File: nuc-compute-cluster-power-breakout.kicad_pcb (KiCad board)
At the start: 4 copper layers, 100 x 100 mm, 169 parts, among them J1 USB3106-30-0230-A, J10 10107844-002LF, J2 BM04B-SRSS-TB-LF-SN, J3 BM04B-SRSS-TB-LF-SN, J4 43045-1013, J5 430450812, J6 430450812, J7 430450812, J8 430450812, J9 430450812, Q1 SQS401EN-T1_BE3, Q10 SSM3K15ACT, Q11 BC856,215, Q2 SQS401EN-T1_BE3, Q3 SSM3K15ACT, Q4 SSM3K15ACT, Q5 SQS401EN-T1_BE3, Q6 SSM3K15ACT, Q7 SQS401EN-T1_BE3, Q8 SQS401EN-T1_BE3, Q9 SSM3K15ACT, U1 FT2232HL-REEL, U10 TCA9534, U11 TMCS1100A2-Q1, U12 TMCS1100A2-Q1, U13 TMCS1100A2-Q1, U14 ADS7828, U15 AP62301WU-7, U2 ISO1641, U3 NCP163ASN330T1G, U4 AP62301WU-7, U8 TMCS1100A2-Q1, U9 TMCS1100A2-Q1, Y1 KX-7_12,MHz

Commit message: Performed loclib
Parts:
- C16, C18, C19, C20: footprint antmicro-footprints:0402-cap -> nuc-compute-cluster-power-breakout-footprints:0402-cap
- N1: footprint antmicro-footprints:OSHW-Logo_7.5x8mm_Mask -> nuc-compute-cluster-power-breakout-footprints:OSHW-Logo_7.5x8mm_Mask
- N2: footprint antmicro-footprints:antmicro-logo_scaled_20mm_mask -> nuc-compute-cluster-power-breakout-footprints:antmicro-logo_scaled_20mm_mask
- R11, R12, R36, R37: footprint antmicro-footprints:0402-res -> nuc-compute-cluster-power-breakout-footprints:0402-res
- TP_S1, TP_S10, TP_S11, TP_S12, TP_S16, TP_S17, TP_S18, TP_S19, TP_S2, TP_S20, TP_S21, TP_S22, TP_S23, TP_S24, TP_S3, TP_S4, TP_S5, TP_S6, TP_S7, TP_S8, TP_S9, TP_S_ON1: footprint antmicro-footprints:Testpoint_smd_1mm -> nuc-compute-cluster-power-breakout-footprints:Testpoint_smd_1mm
- U14: footprint antmicro-footprints:TSSOP-16_4.4x5mm_P0.65mm -> nuc-compute-cluster-power-breakout-footprints:TSSOP-16_4.4x5mm_P0.65mm
- U2: footprint antmicro-footprints:SOIC-8_W3.9mm -> nuc-compute-cluster-power-breakout-footprints:SOIC-8_W3.9mm
- U3: footprint antmicro-footprints:SOT-23-5 -> nuc-compute-cluster-power-breakout-footprints:SOT-23-5

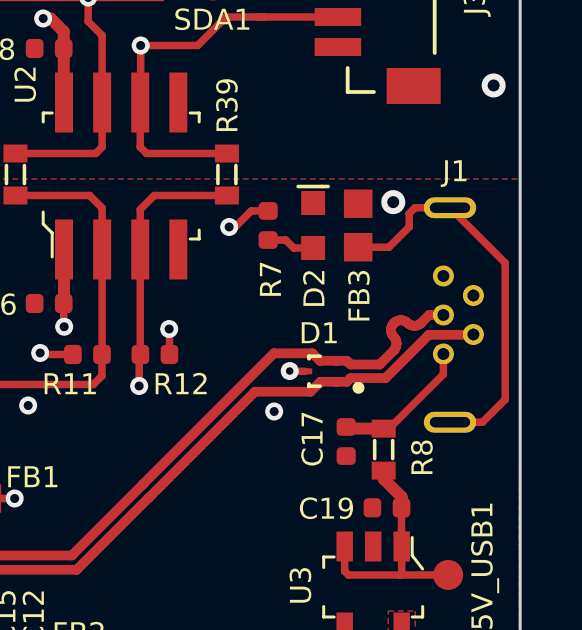
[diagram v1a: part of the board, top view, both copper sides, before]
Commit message: Update USB port footprint
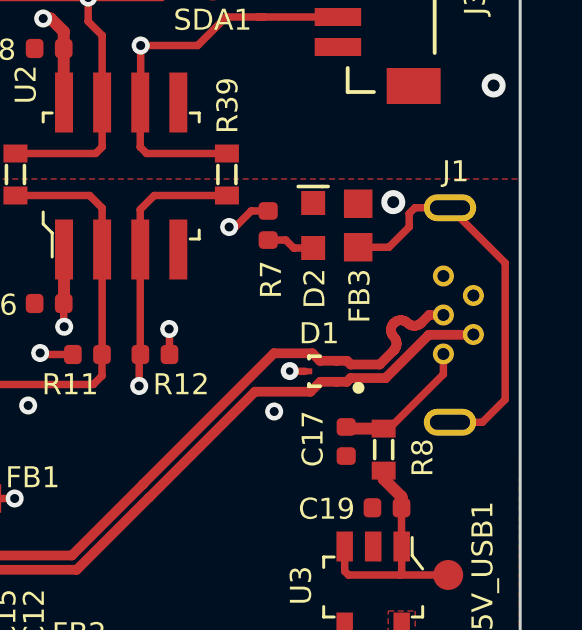
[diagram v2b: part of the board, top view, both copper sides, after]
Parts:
- C16, C18, C19, C20: footprint nuc-compute-cluster-power-breakout-footprints:0402-cap -> antmicro-footprints:0402-cap
- N1: footprint nuc-compute-cluster-power-breakout-footprints:OSHW-Logo_7.5x8mm_Mask -> antmicro-footprints:OSHW-Logo_7.5x8mm_Mask
- N2: footprint nuc-compute-cluster-power-breakout-footprints:antmicro-logo_scaled_20mm_mask -> antmicro-footprints:antmicro-logo_scaled_20mm_mask
- R11, R12, R36, R37: footprint nuc-compute-cluster-power-breakout-footprints:0402-res -> antmicro-footprints:0402-res
- TP_S1, TP_S10, TP_S11, TP_S12, TP_S16, TP_S17, TP_S18, TP_S19, TP_S2, TP_S20, TP_S21, TP_S22, TP_S23, TP_S24, TP_S3, TP_S4, TP_S5, TP_S6, TP_S7, TP_S8, TP_S9, TP_S_ON1: footprint nuc-compute-cluster-power-breakout-footprints:Testpoint_smd_1mm -> antmicro-footprints:Testpoint_smd_1mm
- U14: footprint nuc-compute-cluster-power-breakout-footprints:TSSOP-16_4.4x5mm_P0.65mm -> antmicro-footprints:TSSOP-16_4.4x5mm_P0.65mm
- U2: footprint nuc-compute-cluster-power-breakout-footprints:SOIC-8_W3.9mm -> antmicro-footprints:SOIC-8_W3.9mm
- U3: footprint nuc-compute-cluster-power-breakout-footprints:SOT-23-5 -> antmicro-footprints:SOT-23-5

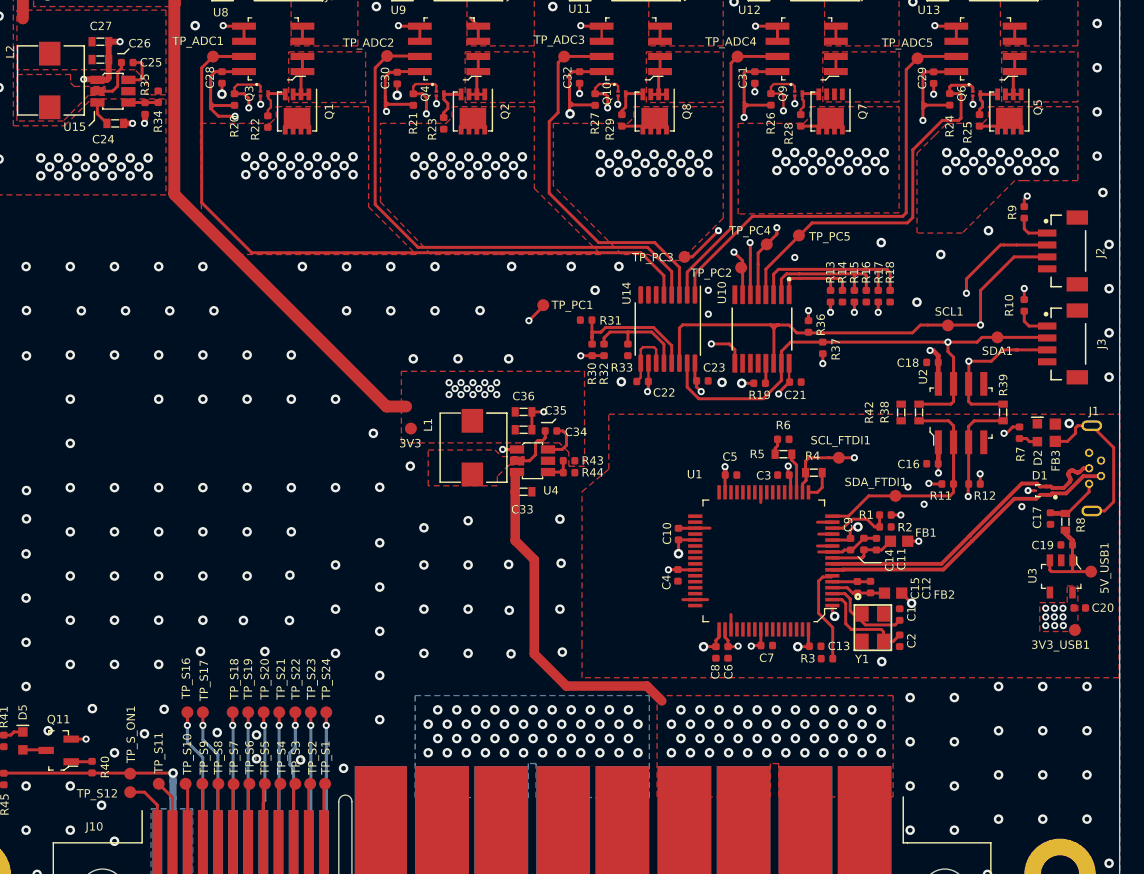
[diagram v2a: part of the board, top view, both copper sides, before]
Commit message: Transistors orientation fix
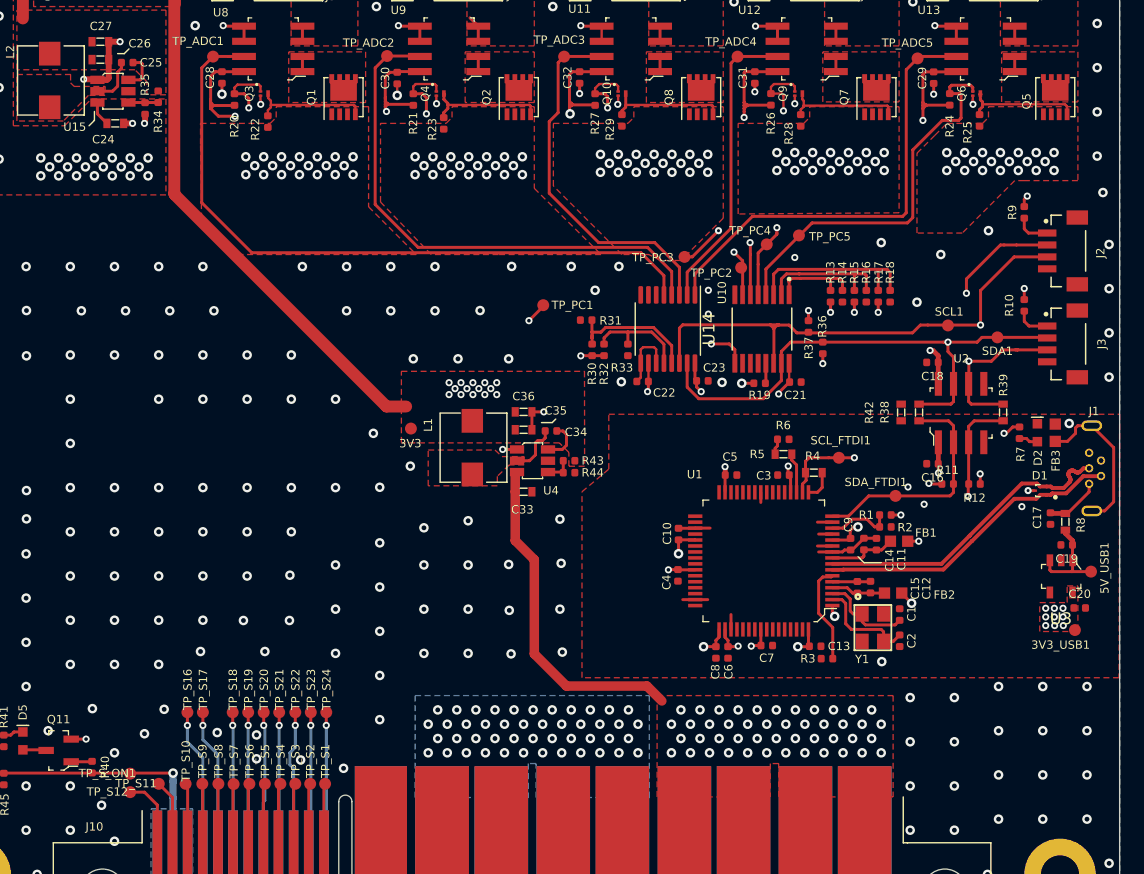
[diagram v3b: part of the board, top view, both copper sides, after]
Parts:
- C16, C18, C19, C20: footprint antmicro-footprints:0402-cap -> nuc-compute-cluster-power-breakout-footprints:0402-cap
- R11, R12, R36, R37: footprint antmicro-footprints:0402-res -> nuc-compute-cluster-power-breakout-footprints:0402-res
- TP_S1, TP_S10, TP_S11, TP_S12, TP_S16, TP_S17, TP_S18, TP_S19, TP_S2, TP_S20, TP_S21, TP_S22, TP_S23, TP_S24, TP_S3, TP_S4, TP_S5, TP_S6, TP_S7, TP_S8, TP_S9, TP_S_ON1: footprint antmicro-footprints:Testpoint_smd_1mm -> nuc-compute-cluster-power-breakout-footprints:Testpoint_smd_1mm
- U14: footprint antmicro-footprints:TSSOP-16_4.4x5mm_P0.65mm -> nuc-compute-cluster-power-breakout-footprints:TSSOP-16_4.4x5mm_P0.65mm
- U2: footprint antmicro-footprints:SOIC-8_W3.9mm -> nuc-compute-cluster-power-breakout-footprints:SOIC-8_W3.9mm
- U3: footprint antmicro-footprints:SOT-23-5 -> nuc-compute-cluster-power-breakout-footprints:SOT-23-5
- moved Q1 4.08 mm to (124.9, 79.8), turned to 90 degrees
- moved Q8 4.08 mm to (154.9, 79.8), turned to 90 degrees
- moved Q2 4.03 mm to (139.6, 79.8), turned to 90 degrees
- moved Q5 4.03 mm to (184.6, 79.8), turned to 90 degrees
- moved Q7 4.03 mm to (169.6, 79.8), turned to 90 degrees
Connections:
- Q1 pad 1: C_MEAS_1 -> VCC12V0
- Q1 pad 2: C_MEAS_1 -> VCC12V0
- Q1 pad 3: C_MEAS_1 -> VCC12V0
- Q1 pad 5: VCC12V0 -> C_MEAS_1
- Q2 pad 1: C_MEAS_2 -> VCC12V0
- Q2 pad 2: C_MEAS_2 -> VCC12V0
- Q2 pad 3: C_MEAS_2 -> VCC12V0
- Q2 pad 5: VCC12V0 -> C_MEAS_2
- Q5 pad 1: C_MEAS_5 -> VCC12V0
- Q5 pad 2: C_MEAS_5 -> VCC12V0
- Q5 pad 3: C_MEAS_5 -> VCC12V0
- Q5 pad 5: VCC12V0 -> C_MEAS_5
- Q7 pad 1: C_MEAS_4 -> VCC12V0
- Q7 pad 2: C_MEAS_4 -> VCC12V0
- Q7 pad 3: C_MEAS_4 -> VCC12V0
- Q7 pad 5: VCC12V0 -> C_MEAS_4
- Q8 pad 1: C_MEAS_3 -> VCC12V0
- Q8 pad 2: C_MEAS_3 -> VCC12V0
- Q8 pad 3: C_MEAS_3 -> VCC12V0
- Q8 pad 5: VCC12V0 -> C_MEAS_3
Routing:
- net VCC12V0: track 57.0 -> 47.8 mm
- net Net-(Q7-Pad4): track 3.32 -> 10.2 mm
- net Net-(Q10-Pad3): track 3.37 -> 9.98 mm
- net Net-(Q5-Pad4): track 3.51 -> 9.96 mm
- net Net-(Q1-Pad4): track 3.53 -> 9.88 mm
- net Net-(Q2-Pad4): track 3.77 -> 10.1 mm
- net C_MEAS_2: track 4.72 -> 1.44 mm
- net C_MEAS_5: track 4.55 -> 1.44 mm
- net C_MEAS_3: track 4.55 -> 1.44 mm
- net C_MEAS_1: track 4.55 -> 1.44 mm
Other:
- board text added: "Rev. 1.1.0"
- board text removed: "Rev. 1.0.0"

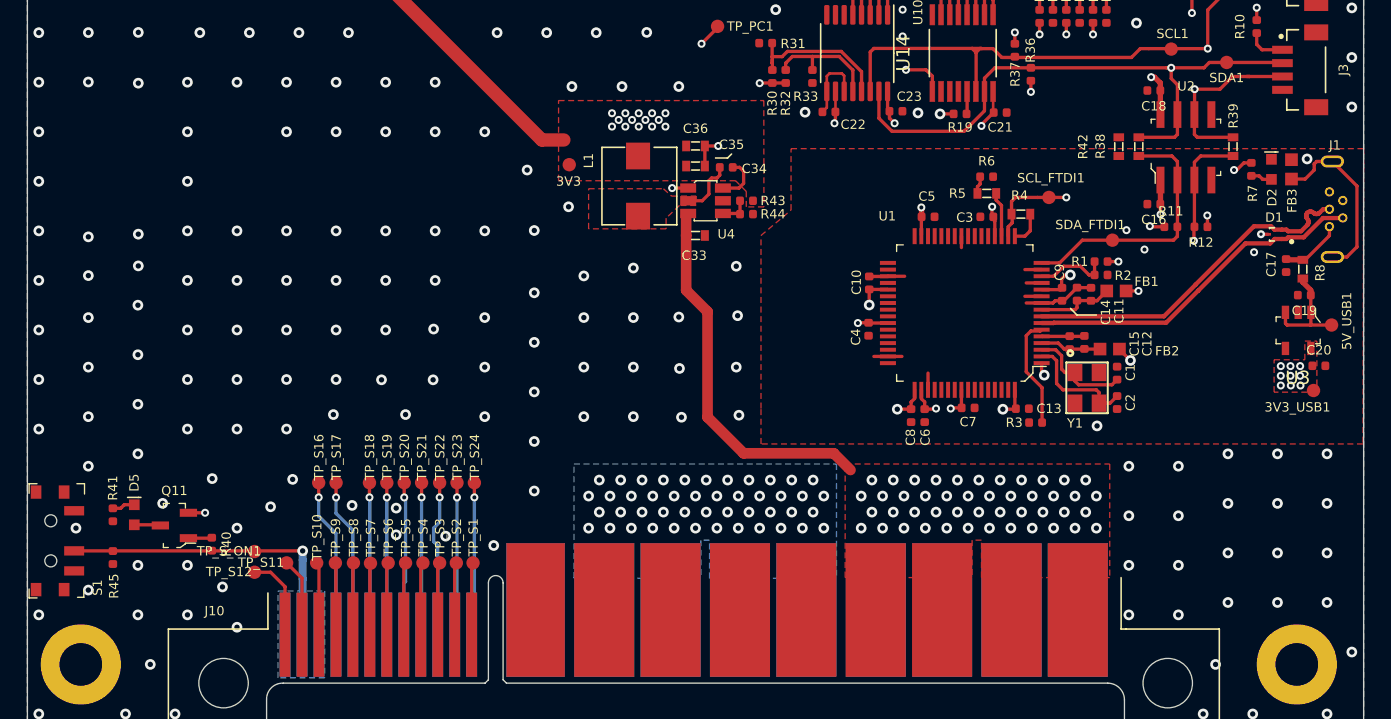
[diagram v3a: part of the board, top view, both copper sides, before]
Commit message: Fixed swapped I2C lines Corrected silkscreen layer Rearranged EdgeConn test points
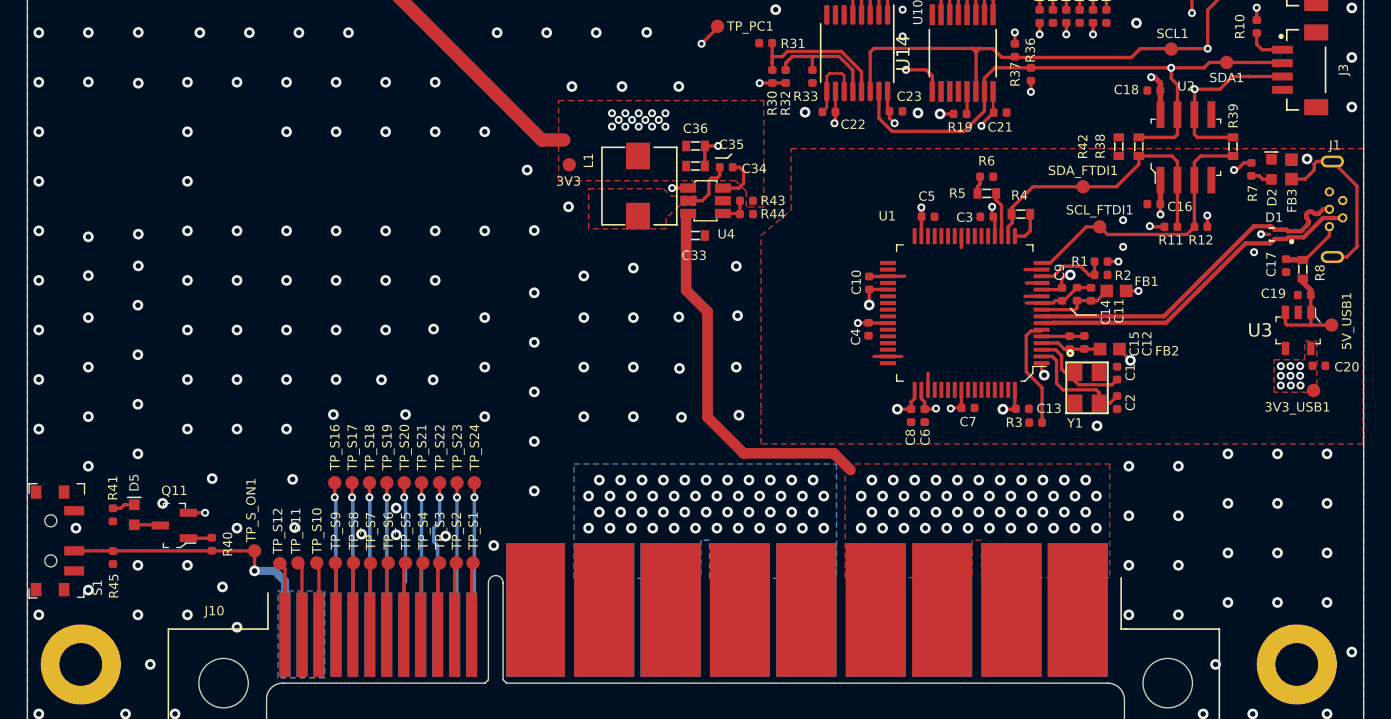
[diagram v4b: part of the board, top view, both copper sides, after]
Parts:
- moved SDA_FTDI1 4.56 mm to (169.0, 109.3)
- moved SCL_FTDI1 4.39 mm to (170.2, 112.3)
- moved TP_S12 2.01 mm to (108.9, 137.5)
- moved TP_S16 1.20 mm to (112.9, 131.4)
- moved TP_S17 1.20 mm to (114.2, 131.4)
- moved TP_S11 0.85 mm to (110.2, 137.5)
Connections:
- R4 pad 2: SCL_FTDI -> SDA_FTDI
- U1 pad 16: SDA_FTDI -> SCL_FTDI
- U1 pad 18: SCL_FTDI -> SDA_FTDI
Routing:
- net SCL_FTDI: track 26.9 -> 21.0 mm, vias 2 -> 0
- net SDA_FTDI: track 19.6 -> 21.7 mm
- net PSU_ON: track 23.1 -> 21.7 mm
- net Net-(J10-PadS12): track 6.32 -> 5.48 mm

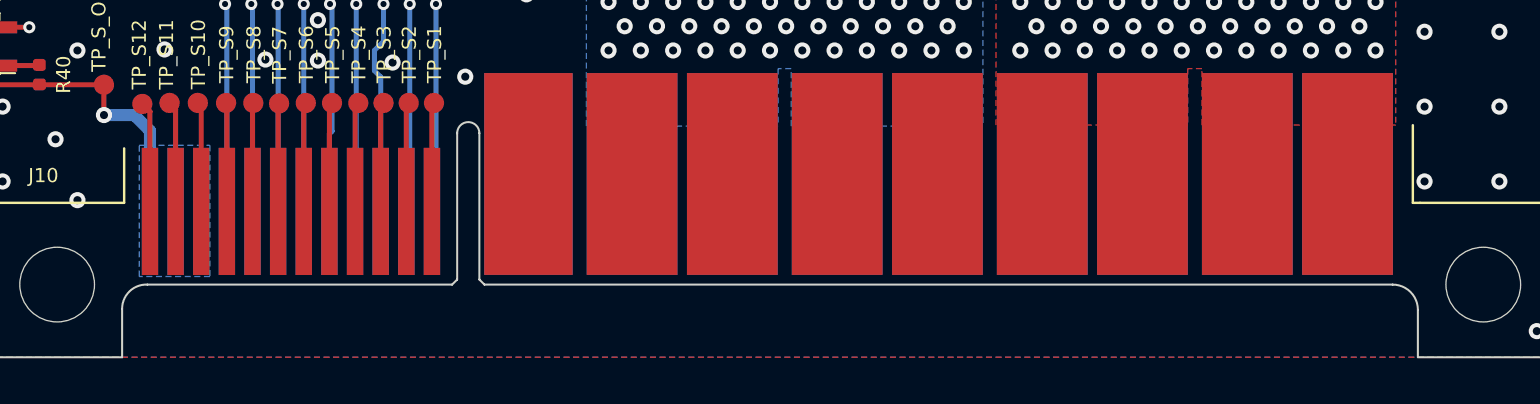
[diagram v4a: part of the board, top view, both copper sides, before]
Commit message: Update project to Kicad 6
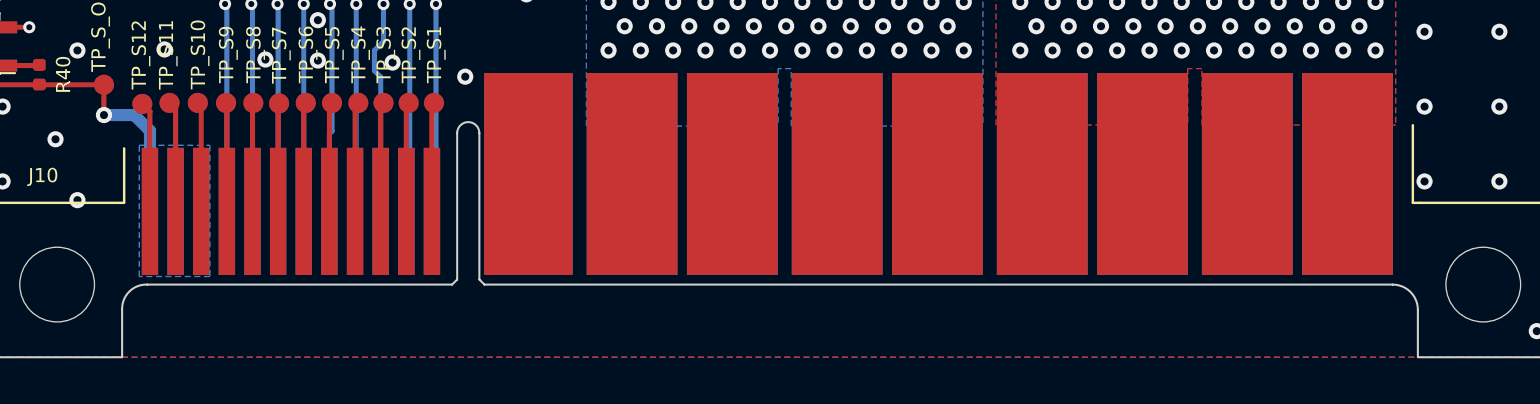
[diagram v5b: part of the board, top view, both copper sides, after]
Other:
- net class Default removed
- net class USB_Diff removed
